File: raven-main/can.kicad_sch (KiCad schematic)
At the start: 7 parts, among them U4 OPA656UB, U5 TLV3201AIDCKT

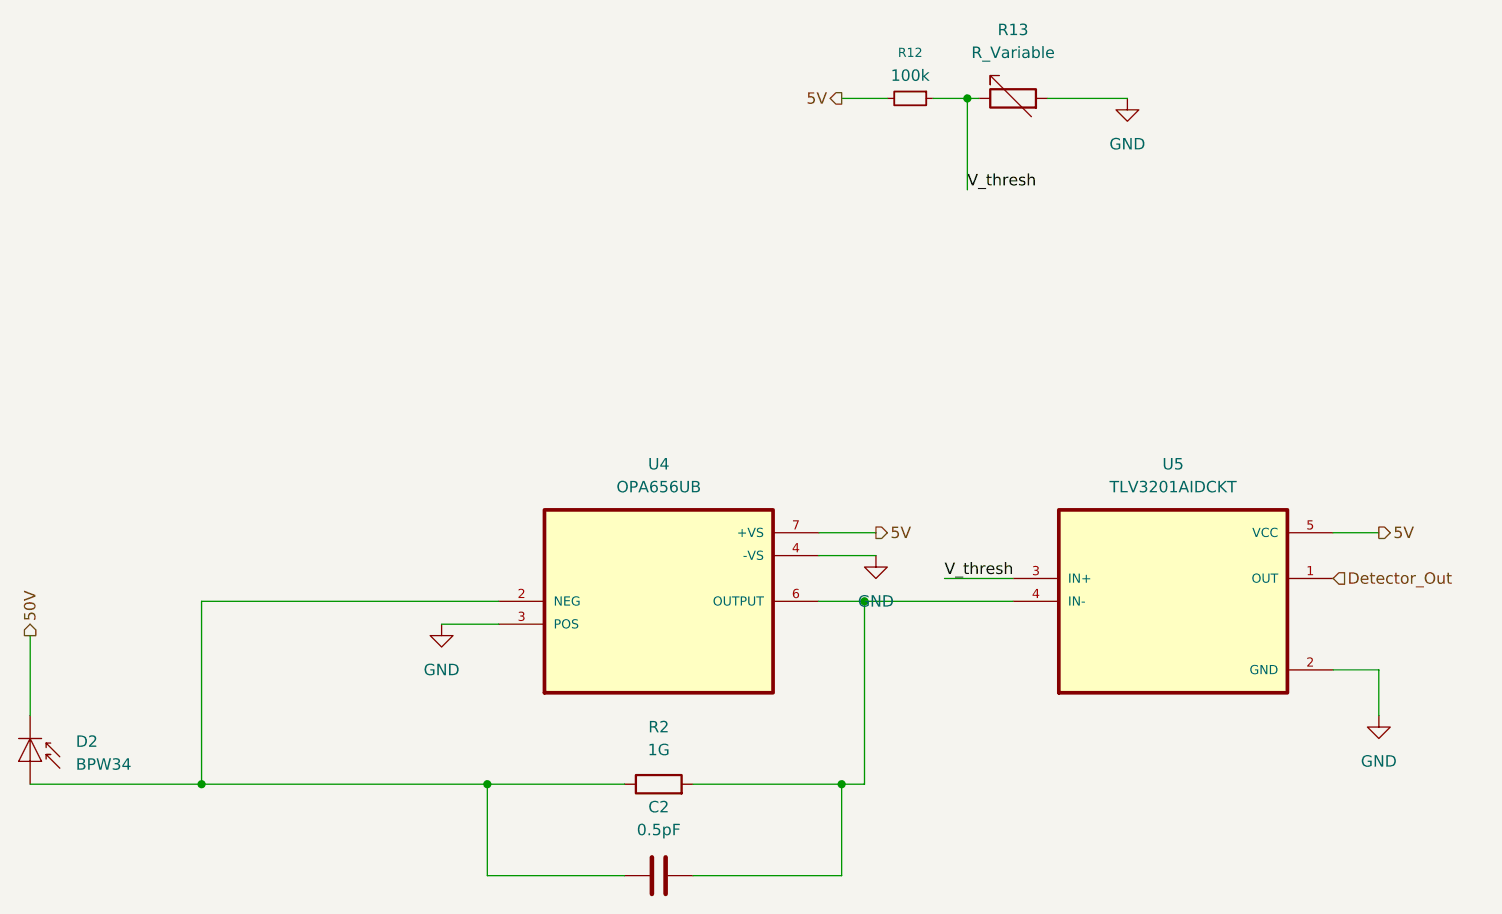
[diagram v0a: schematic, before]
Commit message: Used the ESP-32 board template to create full board
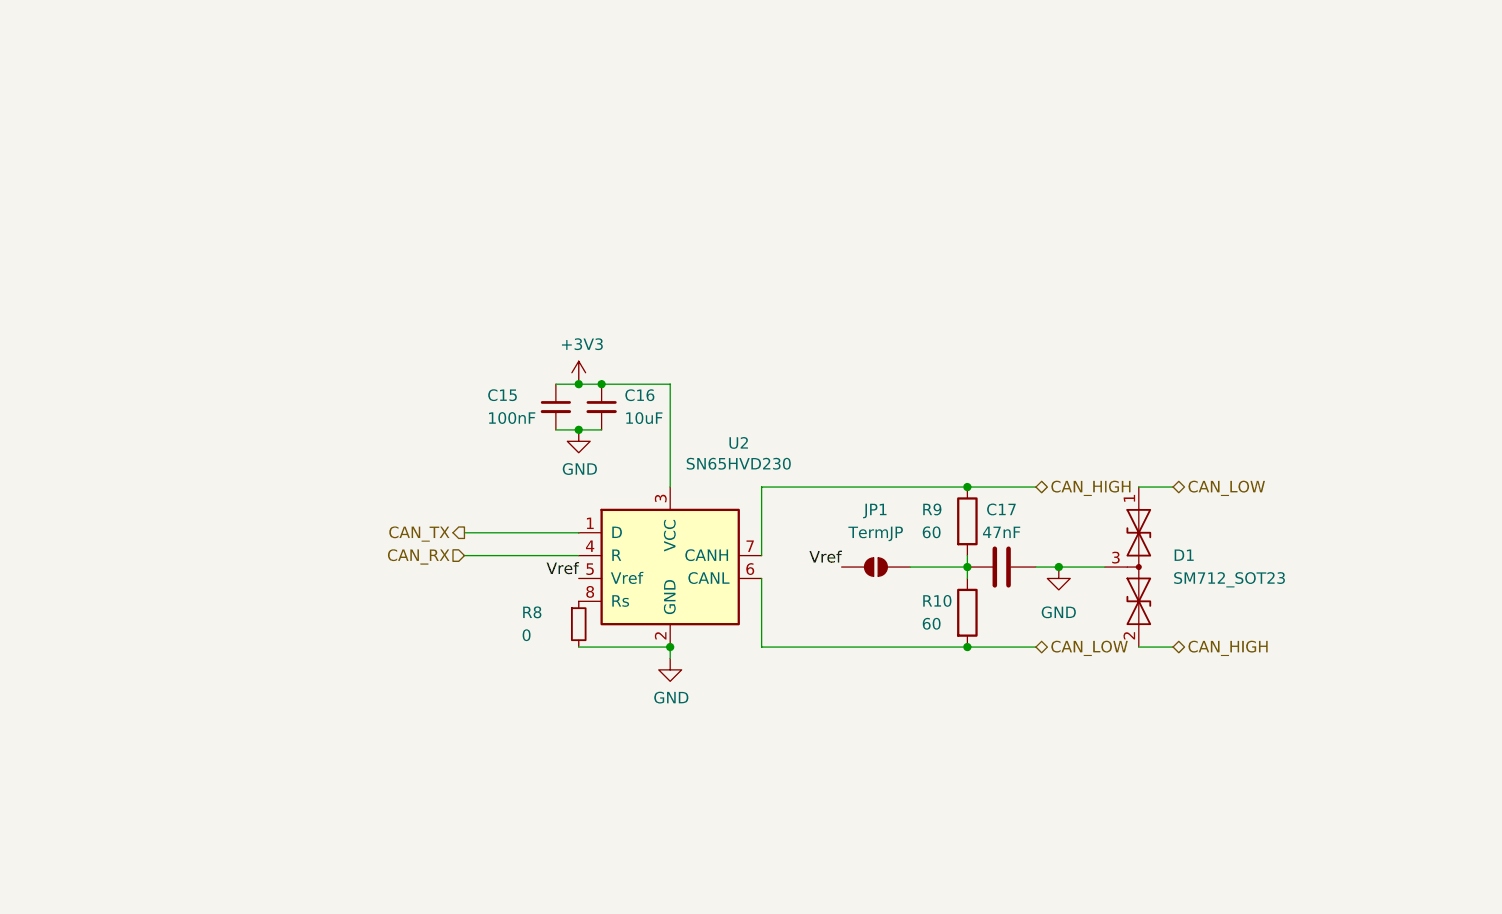
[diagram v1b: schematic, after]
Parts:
- removed C2: 0.5pF, symbol Device:C
- removed D2: BPW34, OptoDevice:Osram_DIL2_4.3x4.65mm_P5.08mm, symbol Sensor_Optical:BPW34
- removed R12: 100k, symbol Device:R_Small
- removed R13: R_Variable, symbol Device:R_Variable
- removed R2: 1G, symbol Device:R
- removed U4: OPA656UB, OPA656UB:SOIC127P599X175-8N, symbol OPA656UB:OPA656UB
- removed U5: TLV3201AIDCKT, TLV3201AIDCKT:SOT65P210X110-5N, symbol TLV3201AIDCKT:TLV3201AIDCKT
- added C15: 100nF, Capacitor_SMD:C_0402_1005Metric, symbol Device:C_Small
- added C16: 10uF, Capacitor_SMD:C_0402_1005Metric, symbol Device:C_Small
- added C17: 47nF, Capacitor_SMD:C_0402_1005Metric, symbol Device:C
- added D1: SM712_SOT23, Package_TO_SOT_SMD:SOT-23, symbol Diode:SM712_SOT23
- added JP1: TermJP, iclr:SmallerSolderJP, symbol Jumper:SolderJumper_2_Open
- added R10, R9: 60, Resistor_SMD:R_0603_1608Metric, symbol Device:R
- added R8: 0, Resistor_SMD:R_0603_1608Metric, symbol Device:R_Small
- added U2: SN65HVD230, Package_SO:SOIC-8_3.9x4.9mm_P1.27mm, symbol Interface_CAN_LIN:SN65HVD230
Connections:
- net GND: now also C15.2, C16.2, C17.2, D1.3 (common), R8.2, U2.2 (GND)
- new net: R8.1, U2.8 (Rs)
- new net: C17.1, JP1.2 (B), R10.1, R9.2
- new net +3V3: C15.1, C16.1, U2.3 (VCC)
- new net CAN_HIGH: D1.2 (A2), R9.1, U2.7 (CANH)
- new net CAN_LOW: D1.1 (A1), R10.2, U2.6 (CANL)
- new net CAN_RX: U2.4 (R)
- new net CAN_TX: U2.1 (D)
- new net Vref: JP1.1 (A), U2.5 (Vref)
